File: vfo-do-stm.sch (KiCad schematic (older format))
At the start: 36 parts, among them J1 DC_in, J2 SWIM, J3 VFO, J4 LO, SW1 SW_FreqMinus, SW2 SW_FreqPlus, SW3 SW_Band, SW4 SW_Res, SW5 SW_NRST, U1 L7805, U2 LP3982IMM-3.3, U3 STM8S208C8, U4 LP3982IMM-3.3, U5 LP3982IMM-3.3, U6 Si5351A-B-GT

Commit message: Ebauche pcb + ajouts schema
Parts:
- removed C14: CP_Small, symbol Device:CP_Small
- added C15: 0.47µF, Capacitor_SMD:C_0805_2012Metric_Pad1.15x1.40mm_HandSolder, symbol Device:C_Small
- added D1: D_Schottky, Diode_SMD:D_0805_2012Metric_Pad1.15x1.40mm_HandSolder, symbol Device:D_Schottky
- C10: renamed from C13; footprint (none) -> Capacitor_SMD:C_0805_2012Metric_Pad1.15x1.40mm_HandSolder
- C14: renamed from C15; value C_Small -> 0.47µF; footprint (none) -> Capacitor_SMD:C_0805_2012Metric_Pad1.15x1.40mm_HandSolder
- C9: renamed from C12; footprint (none) -> Capacitor_SMD:C_0805_2012Metric_Pad1.15x1.40mm_HandSolder
- J1: renamed from J2; footprint (none) -> Connector_Molex:Molex_KK-254_AE-6410-04A_1x04_P2.54mm_Vertical
- J3: renamed from J4; footprint (none) -> Connector_Coaxial:SMA_Molex_73251-2200_Horizontal
- J4: renamed from J3; footprint (none) -> Connector_Coaxial:SMA_Molex_73251-2200_Horizontal
- R4, R5, R6: renamed from R?; footprint (none) -> Resistor_SMD:R_0805_2012Metric_Pad1.15x1.40mm_HandSolder
- SW1, SW2, SW3, SW4, SW5: footprint (none) -> Button_Switch_SMD:SW_Push_1P1T-MP_NO_Horizontal_Alps_SKRTLAE010
- renumbered C9 to C11, C10 to C12, C11 to C13, J1 to J2
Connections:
- net 3.3MCU: now also C15.1
- net GND: now also C15.2
- net at C3.1, U1.1 (IN): now also D1.1 (K); no longer J2.1
- net CLK0: now reaches R4.1
- new net: D1.2 (A), J2.1
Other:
- moved on the sheet: C14, C3, C4, J4, R4, R6, U1

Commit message: Améliorations ébauche PCB
Ajout contour
Changement d'empreinte pour D1, J3, J4
Certains filtrages, découplages, résistance pullup/polldown sont encore manquants.
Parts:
- D1: footprint Diode_SMD:D_0805_2012Metric_Pad1.15x1.40mm_HandSolder -> Diode_SMD:D_SMA-SMB_Universal_Handsoldering
- J1: footprint Connector_Molex:Molex_KK-254_AE-6410-04A_1x04_P2.54mm_Vertical -> Connector_JST:JST_ZH_B4B-ZR_1x04_P1.50mm_Vertical
- J3, J4: footprint Connector_Coaxial:SMA_Molex_73251-2200_Horizontal -> Connector_Coaxial:SMA_Molex_73251-2120_EdgeMount_Horizontal
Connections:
- net Net_5.5V: now reaches C1.1, C11.1, C4.1, C6.1, U1.3 (OUT), U2.2 (IN), U2.7 (~SHDN), U4.2 (IN), U5.2 (IN)
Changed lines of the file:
@@
 F 0 "J1" V 10664 462 50  0000 R CNN
 F 1 "SWIM" V 10573 462 50  0000 R CNN
-F 2 "Connector_Molex:Molex_KK-254_AE-6410-04A_1x04_P2.54mm_Vertical" H 10700 750 50  0001 C CNN
+F 2 "Connector_JST:JST_ZH_B4B-ZR_1x04_P1.50mm_Vertical" H 10700 750 50  0001 C CNN
 F 3 "~" H 10700 750 50  0001 C CNN
 	1    10700 750
@@
 F 0 "J4" V 3232 7400 50  0000 L CNN
 F 1 "VFO" V 3323 7400 50  0000 L CNN
-F 2 "Connector_Coaxial:SMA_Molex_73251-2200_Horizontal" H 3350 7300 50  0001 C CNN
+F 2 "Connector_Coaxial:SMA_Molex_73251-2120_EdgeMount_Horizontal" H 3350 7300 50  0001 C CNN
 F 3 " ~" H 3350 7300 50  0001 C CNN
 	1    3350 7300
@@
 F 0 "J3" H 2700 7275 50  0000 L CNN
 F 1 "LO" H 2700 7184 50  0000 L CNN
-F 2 "Connector_Coaxial:SMA_Molex_73251-2200_Horizontal" H 2600 7300 50  0001 C CNN
+F 2 "Connector_Coaxial:SMA_Molex_73251-2120_EdgeMount_Horizontal" H 2600 7300 50  0001 C CNN
 F 3 " ~" H 2600 7300 50  0001 C CNN
 	1    2600 7300
@@
 F 0 "D1" H 1650 783 50  0000 C CNN
 F 1 "D_Schottky" H 1650 874 50  0000 C CNN
-F 2 "Diode_SMD:D_0805_2012Metric_Pad1.15x1.40mm_HandSolder" H 1650 1000 50  0001 C CNN
+F 2 "Diode_SMD:D_SMA-SMB_Universal_Handsoldering" H 1650 1000 50  0001 C CNN
 F 3 "~" H 1650 1000 50  0001 C CNN
 	1    1650 1000
@@
 	1350 1000 1500 1000
 Connection ~ 1350 1000
+Text Label 3250 1000 0    50   ~ 0
+Net_5.5V
 $EndSCHEMATC

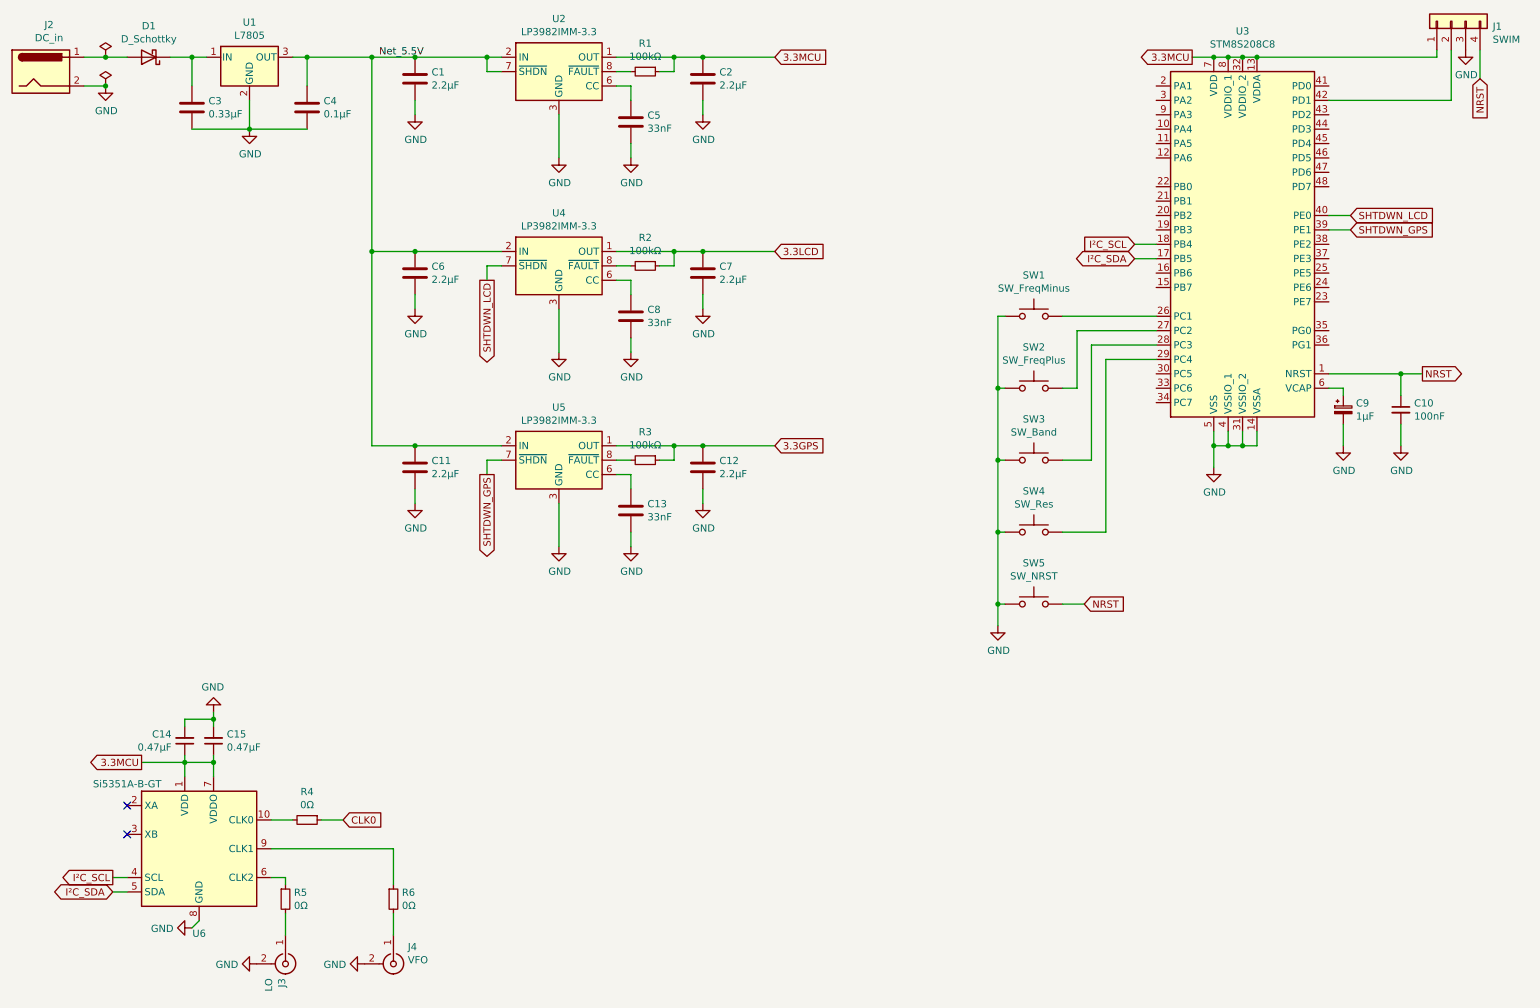
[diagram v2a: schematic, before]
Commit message: Ebauche ecran
Ajout connecteur pour afficheur oled https://www.buydisplay.com/yellow-2-4-inch-graphic-oled-display-128x64-serial-spi-i2c-ssd1309
Renommage nets GPS -> CLK
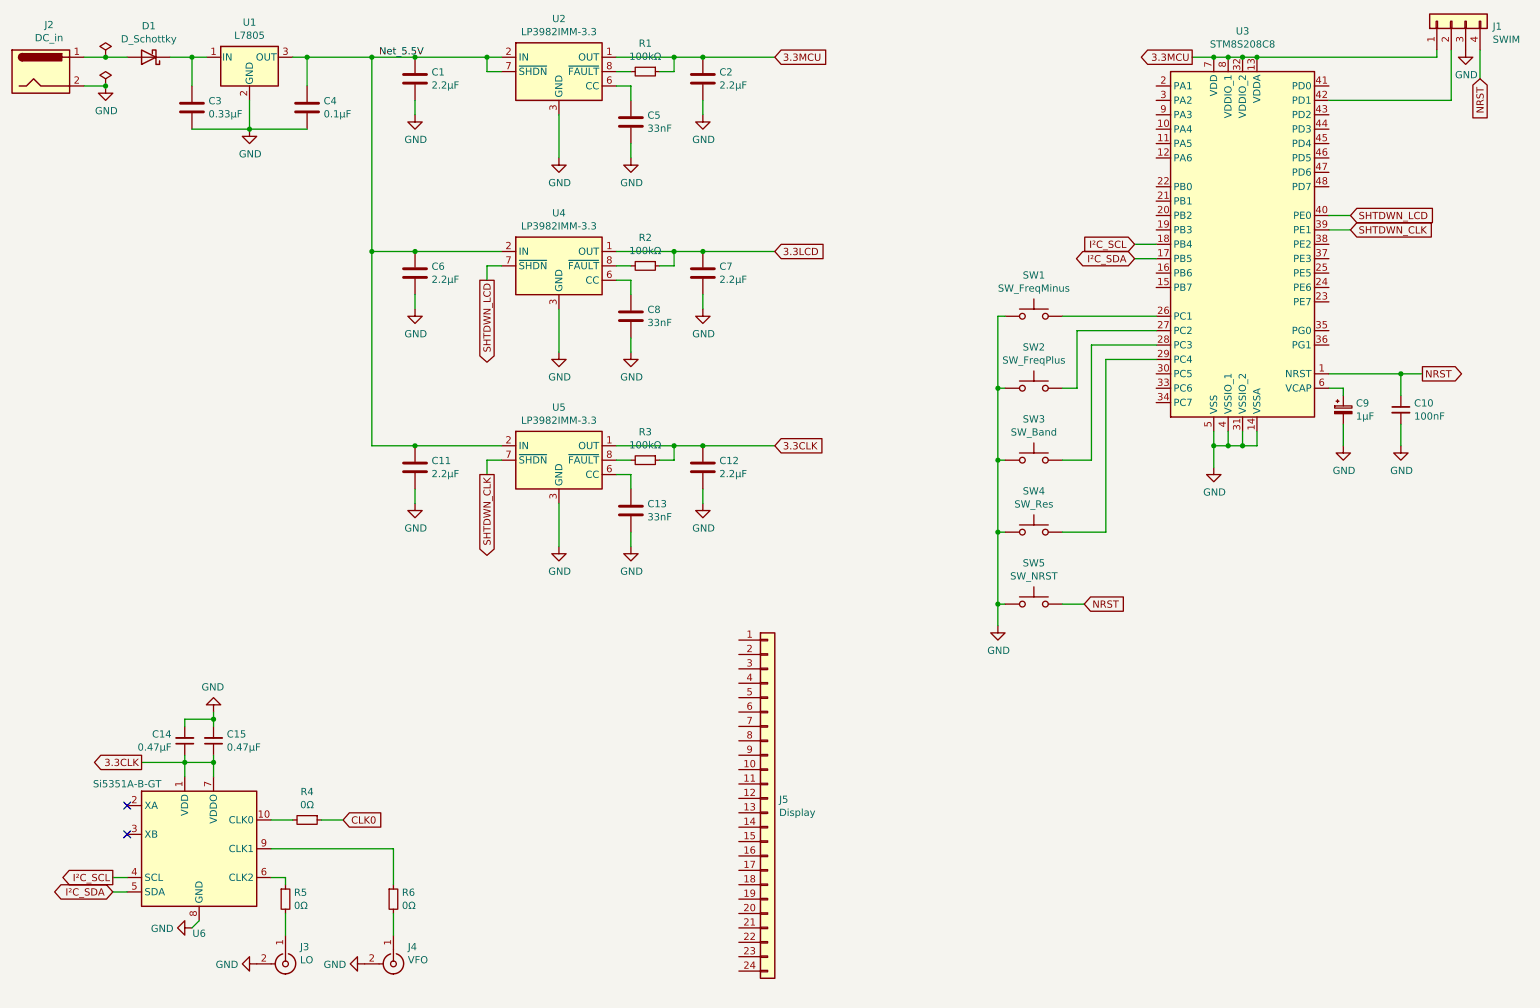
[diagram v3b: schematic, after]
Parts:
- added J5: Display, Connector_FFC-FPC:Molex_52435-2433_1x24-1MP_P0.5mm_Horizontal_TopContact, symbol Connector_Generic:Conn_01x24
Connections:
- net 3.3MCU: no longer C14.1, C15.1, U6.1 (VDD), U6.7 (VDDO)
- net 3.3GPS renamed 3.3CLK
- net 3.3CLK: now also C14.1, C15.1, U6.1 (VDD), U6.7 (VDDO)
- net SHTDWN_GPS renamed SHTDWN_CLK
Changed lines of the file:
@@
 3.3LCD
 Text GLabel 6000 3700 2    50   Input ~ 0
-3.3GPS
+3.3CLK
 Wire Wire Line
 	6000 2350 5500 2350
@@
 Connection ~ 5500 1000
 Text GLabel 4000 3900 3    50   Output ~ 0
-SHTDWN_GPS
+SHTDWN_CLK
 Wire Wire Line
 	3500 3700 4100 3700
@@
 	4000 3800 4000 3900
 Text GLabel 10000 2200 2    50   Input ~ 0
-SHTDWN_GPS
+SHTDWN_CLK
 Wire Wire Line
 	10000 2200 9850 2200
@@
 	1950 7050 2000 7000
 Text GLabel 1600 5900 0    50   Output ~ 0
-3.3MCU
+3.3CLK
 $Comp
 L Device:C_Small C14
@@
 U 1 1 5F678EA6
 P 2600 7300
-F 0 "J3" H 2700 7275 50  0000 L CNN
-F 1 "LO" H 2700 7184 50  0000 L CNN
+F 0 "J3" V 2482 7401 50  0000 L CNN
+F 1 "LO" V 2573 7401 50  0000 L CNN
 F 2 "Connector_Coaxial:SMA_Molex_73251-2120_EdgeMount_Horizontal" H 2600 7300 50  0001 C CNN
 F 3 " ~" H 2600 7300 50  0001 C CNN
@@
 Text Label 3250 1000 0    50   ~ 0
 Net_5.5V
+$Comp
+L Connector_Generic:Conn_01x24 J5
+U 1 1 5F3F08EC
+P 5950 6150
+F 0 "J5" H 6030 6142 50  0000 L CNN
+F 1 "Display" H 6030 6051 50  0000 L CNN
+F 2 "Connector_FFC-FPC:Molex_52435-2433_1x24-1MP_P0.5mm_Horizontal_TopContact" H 5950 6150 50  0001 C CNN
+F 3 "~" H 5950 6150 50  0001 C CNN
+	1    5950 6150
+	1    0    0    -1
+$EndComp
 $EndSCHEMATC

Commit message: Changement régul 3.3V & ajout expander I²C
Refonte de l'étage d'alim
Ajout d'une extension de 16 I/O en I²C
Retrait du connecteur écran
Ajout d'un crystal 24MHz pour le MCU
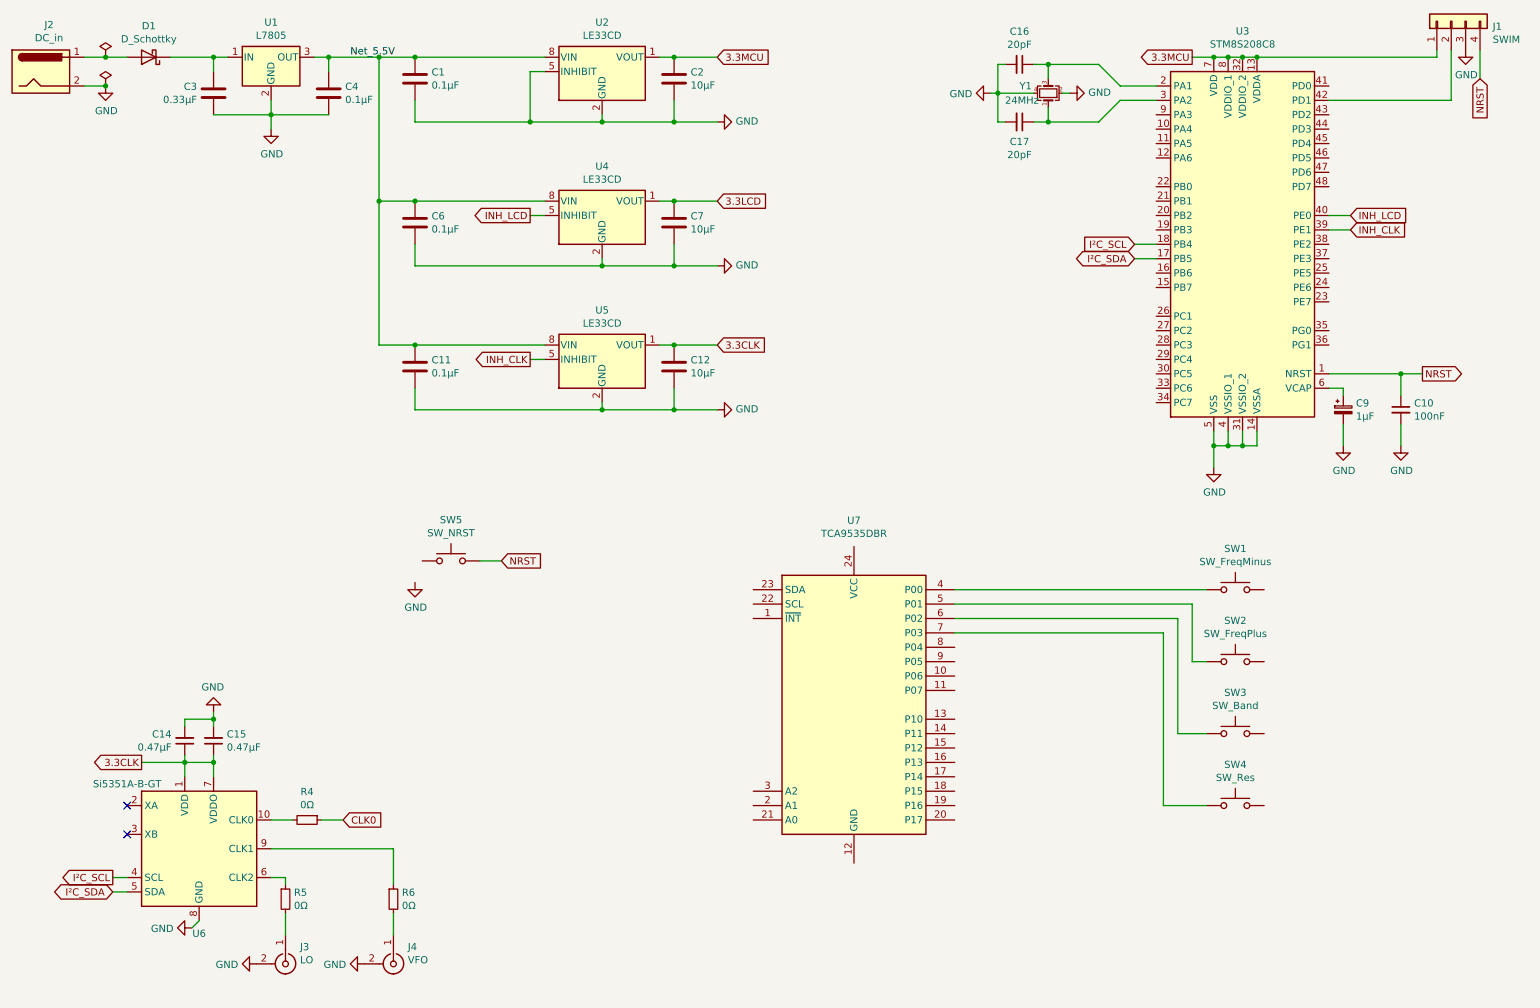
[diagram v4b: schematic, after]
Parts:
- removed C13, C5, C8: 33nF, Capacitor_SMD:C_0805_2012Metric_Pad1.15x1.40mm_HandSolder, symbol Device:C
- removed J5: Display, Connector_FFC-FPC:Molex_52435-2433_1x24-1MP_P0.5mm_Horizontal_TopContact, symbol Connector_Generic:Conn_01x24
- removed R1, R2, R3: 100kΩ, Resistor_SMD:R_0805_2012Metric_Pad1.15x1.40mm_HandSolder, symbol Device:R_Small
- removed U2, U4, U5: LP3982IMM-3.3, Package_SO:VSSOP-8_3.0x3.0mm_P0.65mm, symbol Regulator_Linear:LP3982IMM-3.3
- added C16, C17: 20pF, Capacitor_SMD:C_0805_2012Metric_Pad1.15x1.40mm_HandSolder, symbol Device:C_Small
- added U2, U4, U5: LE33CD, Package_SO:SO-8_3.9x4.9mm_P1.27mm, symbol Regulator_Linear:LE33CD
- added U7: TCA9535DBR, Package_SO:SSOP-24_5.3x8.2mm_P0.65mm, symbol Interface_Expansion:TCA9535DBR
- added Y1: 24MHz, Crystal:Crystal_SMD_2520-4Pin_2.5x2.0mm, symbol Device:Crystal_GND24_Small
- C1, C11, C6: value 2.2µF -> 0.1µF
- C12, C2, C7: value 2.2µF -> 10µF
- J3, J4: footprint Connector_Coaxial:SMA_Molex_73251-2120_EdgeMount_Horizontal -> Connector_Coaxial:SMA_Molex_73251-2200_Horizontal
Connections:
- net 3.3CLK: now also U5.1 (VOUT)
- net 3.3LCD: now also U4.1 (VOUT)
- net 3.3MCU: now also U2.1 (VOUT)
- net GND: now also C16.2, C17.2, U2.2 (GND), U2.3 (GND), U2.5 (INHIBIT), U2.6 (GND), U2.7 (GND), U4.2 (GND), U4.3 (GND), U4.6 (GND), U4.7 (GND), U5.2 (GND), U5.3 (GND), U5.6 (GND), U5.7 (GND), Y1.2, Y1.4; no longer SW1.1, SW2.1, SW3.1, SW4.1, SW5.1
- net Net_5.5V: now also U2.8 (VIN), U4.8 (VIN), U5.8 (VIN)
- net at U3.2 (PA1): now also C16.1, Y1.3
- net at U3.26 (PC1): no longer SW1.2
- net at U3.27 (PC2): no longer SW2.2
- net at U3.28 (PC3): no longer SW3.2
- net at U3.29 (PC4): no longer SW4.2
- net at U3.3 (PA2): now also C17.1, Y1.1
- net SHTDWN_CLK renamed INH_CLK
- net INH_CLK: now also U5.5 (INHIBIT)
- net SHTDWN_LCD renamed INH_LCD
- net INH_LCD: now also U4.5 (INHIBIT)
- new net: SW1.1, U7.4 (P00)
- new net: SW2.1, U7.5 (P01)
- new net: SW3.1, U7.6 (P02)
- new net: SW4.1, U7.7 (P03)
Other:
- moved on the sheet: C11, C12, C2, C3, C4, C6, C7, SW1, SW2, SW3, SW4, SW5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

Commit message: Répartition des éléments du schéma en feuilles hiérarchiques
petites modifs du pcb
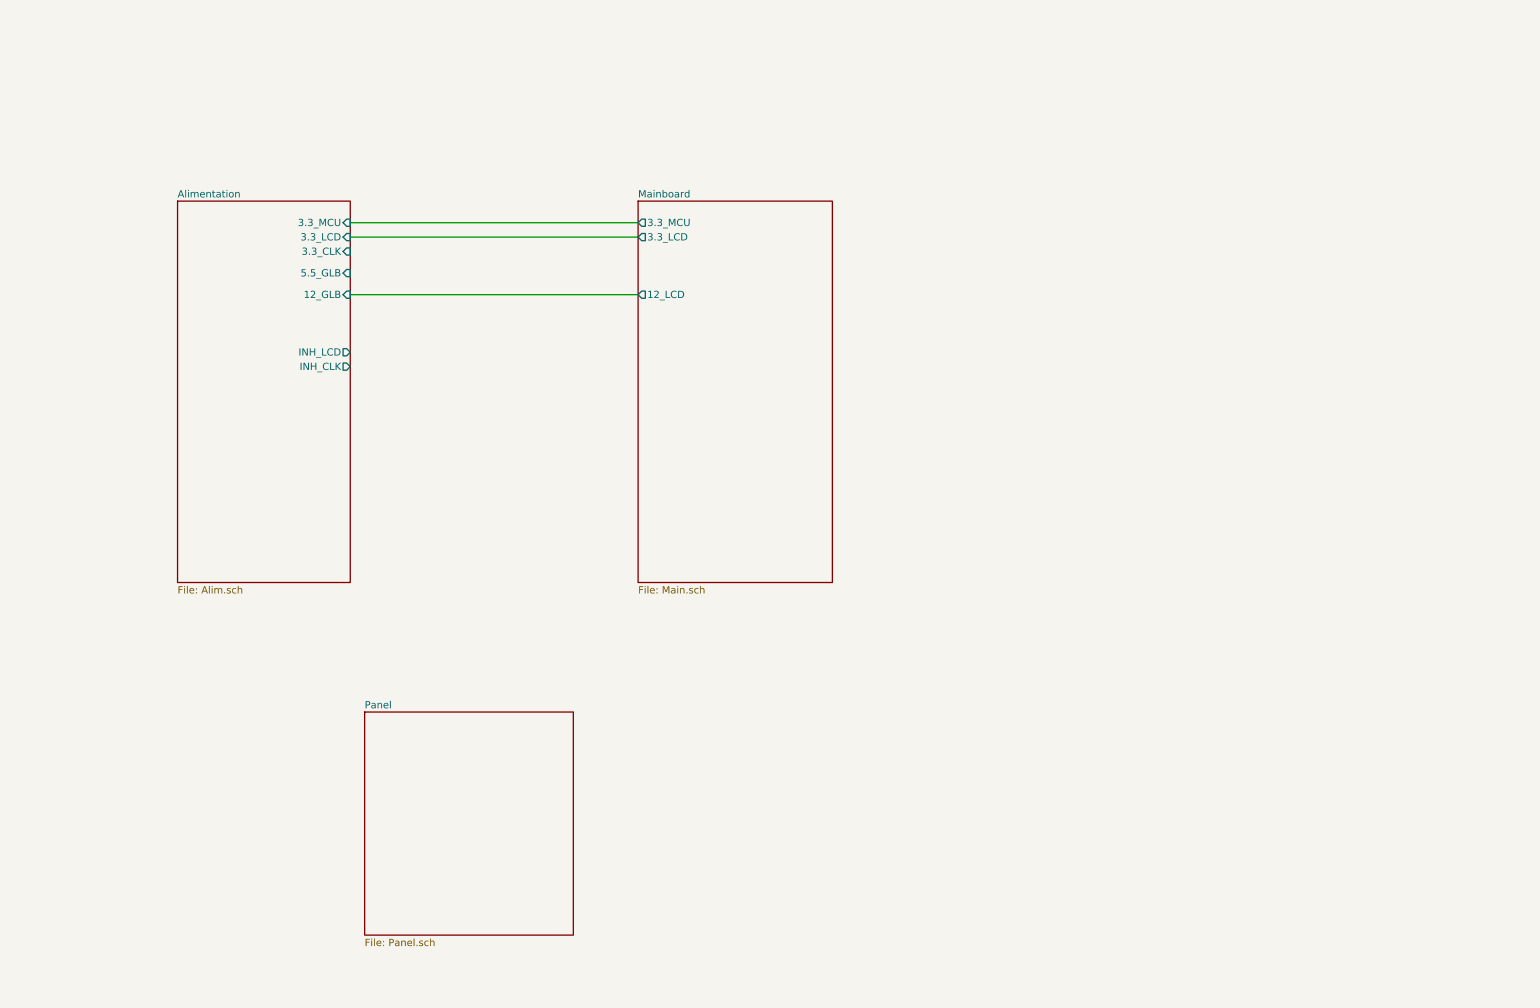
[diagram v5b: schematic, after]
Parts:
- removed C1, C11, C4, C6: 0.1µF, Capacitor_SMD:C_0805_2012Metric_Pad1.15x1.40mm_HandSolder, symbol Device:C
- removed C10: 100nF, Capacitor_SMD:C_0805_2012Metric_Pad1.15x1.40mm_HandSolder, symbol Device:C_Small
- removed C12, C2, C7: 10µF, Capacitor_SMD:C_0805_2012Metric_Pad1.15x1.40mm_HandSolder, symbol Device:C
- removed C14, C15: 0.47µF, Capacitor_SMD:C_0805_2012Metric_Pad1.15x1.40mm_HandSolder, symbol Device:C_Small
- removed C16, C17: 20pF, Capacitor_SMD:C_0805_2012Metric_Pad1.15x1.40mm_HandSolder, symbol Device:C_Small
- removed C3: 0.33µF, Capacitor_SMD:C_0805_2012Metric_Pad1.15x1.40mm_HandSolder, symbol Device:C
- removed C9: 1µF, Capacitor_SMD:C_0805_2012Metric_Pad1.15x1.40mm_HandSolder, symbol Device:CP_Small
- removed D1: D_Schottky, Diode_SMD:D_SMA-SMB_Universal_Handsoldering, symbol Device:D_Schottky
- removed J1: SWIM, Connector_JST:JST_ZH_B4B-ZR_1x04_P1.50mm_Vertical, symbol Connector_Generic:Conn_01x04
- removed J2: DC_in, Connector_BarrelJack:BarrelJack_CUI_PJ-063AH_Horizontal, symbol Connector:Barrel_Jack
- removed J3: LO, Connector_Coaxial:SMA_Molex_73251-2200_Horizontal, symbol Connector:Conn_Coaxial
- removed J4: VFO, Connector_Coaxial:SMA_Molex_73251-2200_Horizontal, symbol Connector:Conn_Coaxial
- removed R4, R5, R6: 0Ω, Resistor_SMD:R_0805_2012Metric_Pad1.15x1.40mm_HandSolder, symbol Device:R_Small
- removed SW1: SW_FreqMinus, Button_Switch_SMD:SW_Push_1P1T-MP_NO_Horizontal_Alps_SKRTLAE010, symbol Switch:SW_Push
- removed SW2: SW_FreqPlus, Button_Switch_SMD:SW_Push_1P1T-MP_NO_Horizontal_Alps_SKRTLAE010, symbol Switch:SW_Push
- removed SW3: SW_Band, Button_Switch_SMD:SW_Push_1P1T-MP_NO_Horizontal_Alps_SKRTLAE010, symbol Switch:SW_Push
- removed SW4: SW_Res, Button_Switch_SMD:SW_Push_1P1T-MP_NO_Horizontal_Alps_SKRTLAE010, symbol Switch:SW_Push
- removed SW5: SW_NRST, Button_Switch_SMD:SW_Push_1P1T-MP_NO_Horizontal_Alps_SKRTLAE010, symbol Switch:SW_Push
- removed U1: L7805, Package_TO_SOT_SMD:TO-263-2, symbol Regulator_Linear:L7805
- removed U2, U4, U5: LE33CD, Package_SO:SO-8_3.9x4.9mm_P1.27mm, symbol Regulator_Linear:LE33CD
- removed U3: STM8S208C8, Package_QFP:LQFP-48_7x7mm_P0.5mm, symbol MCU_ST_STM8:STM8S208C8
- removed U6: Si5351A-B-GT, Package_SO:MSOP-10_3x3mm_P0.5mm, symbol Oscillator:Si5351A-B-GT
- removed U7: TCA9535DBR, Package_SO:SSOP-24_5.3x8.2mm_P0.65mm, symbol Interface_Expansion:TCA9535DBR
- removed Y1: 24MHz, Crystal:Crystal_SMD_2520-4Pin_2.5x2.0mm, symbol Device:Crystal_GND24_Small
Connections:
- no-connect marks 2 -> 0
